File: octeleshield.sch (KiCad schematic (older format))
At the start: 24 parts, among them P1 POWER_HEADER, P2 ANALOG_HEADER, P3 ICSP_HEADER, P4 DIGITAL_HEADER_2, P5 DIGITAL_HEADER_1, P6 V_PROBE2, P7 V_PROBE1, P8 THERMOCOUPLE1, P9 THERMOCOUPLE2, U1 MAX3378E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

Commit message: more work in progress
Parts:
- added C3, C4, C5, C6: 0.1u, Capacitors_SMD:C_0603_HandSoldering, symbol C
- added P7: V_PROBE2_GND, parts:Test_Probe, symbol CONN_01X02
- added P9: V_PROBE1_GND, parts:Test_Probe, symbol CONN_01X02
- C1, C2: footprint (none) -> Capacitors_SMD:C_0603_HandSoldering
- D1, D2, D3, D4: footprint (none) -> Diodes_SMD:SOD-323
- P1, P4, P5: footprint (none) -> Pin_Headers:Pin_Header_Straight_1x08
- P10: renamed from P8; footprint (none) -> parts:Thermocouple
- P11: renamed from P9; footprint (none) -> parts:Thermocouple
- P2: footprint (none) -> Pin_Headers:Pin_Header_Straight_1x06
- P3: footprint (none) -> Socket_Strips:Socket_Strip_Straight_2x03
- P6: value V_PROBE2 -> V_PROBE2_SIG; footprint (none) -> parts:Test_Probe; MFN (none) -> TE Connectivity; MFPN (none) -> 3-582118-2
- P8: renamed from P7; value V_PROBE1 -> V_PROBE1_SIG; footprint (none) -> parts:Test_Probe; MFN (none) -> TE Connectivity; MFPN (none) -> 3-582118-2
- R1, R2, R3, R4, R5, R6: footprint (none) -> Resistors_SMD:R_0603_HandSoldering
- U1: footprint (none) -> Housings_SSOP:TSSOP-14_4.4x5mm_Pitch0.65mm
- U2, U3: footprint SO-8 -> Power_Integrations:SO-8
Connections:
- net +3V3: now also C4.2, C5.2, C6.2
- net +5V: now also P3.5 (P5), C3.1; no longer P3.1 (P1)
- net GND: now also P3.1 (P1), C3.2, C4.1, C5.1, C6.1, P7.1 (P1), P9.1 (P1); no longer P3.5 (P5), P6.2 (P2), P8.2 (P2)
- net MISO: now also P3.6 (P6); no longer P3.2 (P2)
- no-connect marks 23 -> 27

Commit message: work in progress, first try of pcb layout
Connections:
- net +3V3: now also U1.8 (~THREE-STATE)
- net CS1: now also P5.3 (P3); no longer P5.6 (P6)
- net CS2: now also P5.4 (P4); no longer P5.7 (P7)
- net A4: now reaches P2.5 (P5)
- net A4: now also R2.2
- net A5: now reaches P2.6 (P6)
- net A5: now also R1.2
- net A0: no longer names the net of P2.1 (P1)
- net A0: no longer R2.2
- net A1: no longer names the net of P2.2 (P2)
- net A1: no longer R1.2
- net TC_ENABLE: no longer names the net of P5.5 (P5)
- no-connect marks 27 -> 28
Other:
- note added: "4.32:1 voltage divider"
- note added: "Power lines connected to each other within Arduino\n(so e.g. should not wire the two 5V pins to each other)"
- note added: "VCC is higher voltage side, VL is lower voltage side\nThe ~THREE-STATE~ pin is kept high for\nalways normal operation"
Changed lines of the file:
@@
 Sheet 1 1
 Title "Overclocking telemetry shield for Arduino Yún"
-Date "2016-01-11"
+Date "2016-01-17"
 Rev "v1"
 Comp "Moonpunch.org"
@@
 Text Label 6300 2800 2    60   ~ 0
 CS2
-Text Label 6300 2200 2    60   ~ 0
-TC_ENABLE
 Text Label 3050 3650 1    60   ~ 0
 SCLK
@@
 NoConn ~ 4050 2250
 NoConn ~ 4050 2150
-Text Label 4050 3450 0    60   ~ 0
+Text Label 4050 3750 0    60   ~ 0
 CS1
-Text Label 4050 3350 0    60   ~ 0
+Text Label 4050 3650 0    60   ~ 0
 CS2
-Text Label 4050 3550 0    60   ~ 0
-TC_ENABLE
 NoConn ~ 4050 3250
-NoConn ~ 4050 3650
-NoConn ~ 4050 3750
+NoConn ~ 4050 3450
+NoConn ~ 4050 3350
 NoConn ~ 4050 3850
 NoConn ~ 4050 3950
@@
 GND
 NoConn ~ 2000 2950
-Text Label 2000 3850 2    60   ~ 0
-A0
-Text Label 2000 3750 2    60   ~ 0
-A1
+Text Label 2000 3450 2    60   ~ 0
+A4
+Text Label 2000 3350 2    60   ~ 0
+A5
 NoConn ~ 2000 3650
 NoConn ~ 2000 3550
-NoConn ~ 2000 3450
-NoConn ~ 2000 3350
+NoConn ~ 2000 3850
+NoConn ~ 2000 3750
 Text Notes 6150 950  0    157  ~ 31
 Dual thermocouple measurement
 Text Label 7300 5850 2    60   ~ 0
-A0
+A4
 Text Label 7300 4700 2    60   ~ 0
-A1
+A5
 $Comp
 L +5V #PWR01
@@
 NoConn ~ 10100 5950
 NoConn ~ 9450 5950
-Wire Wire Line
-	7600 2350 7850 2350
-Wire Wire Line
-	7850 2350 7850 1500
-Wire Wire Line
-	7850 1500 8450 1500
-Wire Wire Line
-	7800 2350 7800 2900
-Connection ~ 7800 2350
-Wire Wire Line
-	7600 2500 7950 2500
-Wire Wire Line
-	7950 2500 7950 1600
+NoConn ~ 9450 4800
 Wire Wire Line
 	7950 1600 8450 1600
-Wire Wire Line
-	7900 2500 7900 3000
-Connection ~ 7900 2500
 Wire Wire Line
 	7600 2650 8050 2650
@@
 Wire Wire Line
 	10000 4700 10000 4900
-NoConn ~ 9450 4800
+Wire Wire Line
+	7950 2500 7950 1600
+Connection ~ 7900 2500
+Wire Wire Line
+	7600 2500 7950 2500
+Wire Wire Line
+	7900 2500 7900 3000
+Connection ~ 7800 2350
+Wire Wire Line
+	7800 2350 7800 2900
+Wire Wire Line
+	7600 2350 7850 2350
+Wire Wire Line
+	7850 1500 8450 1500
+Wire Wire Line
+	7850 2350 7850 1500
+Text Label 7600 2200 0    60   ~ 0
+3V3
+NoConn ~ 4050 3550
+Text Notes 1650 4600 0    60   ~ 0
+Power lines connected to each other within Arduino\n(so e.g. should not wire the two 5V pins to each other)
+Text Notes 5800 3750 0    60   ~ 0
+VCC is higher voltage side, VL is lower voltage side\nThe ~THREE-STATE~ pin is kept high for\nalways normal operation
+Text Notes 8400 4450 0    60   ~ 0
+4.32:1 voltage divider
 $EndSCHEMATC

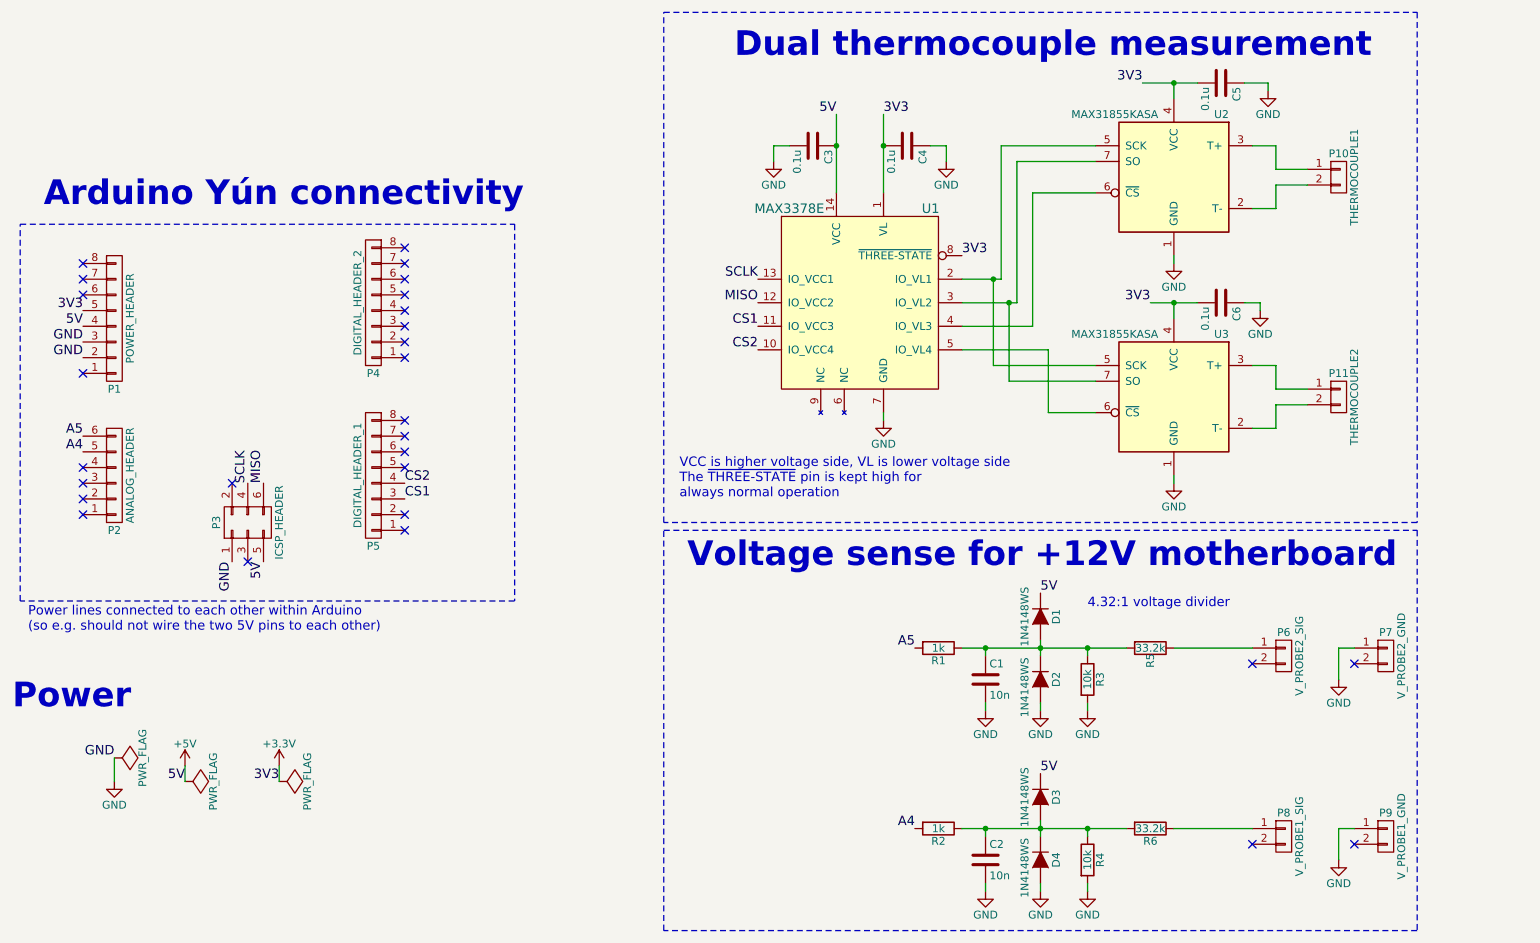
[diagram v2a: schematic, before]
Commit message: some markup and gerber output directory
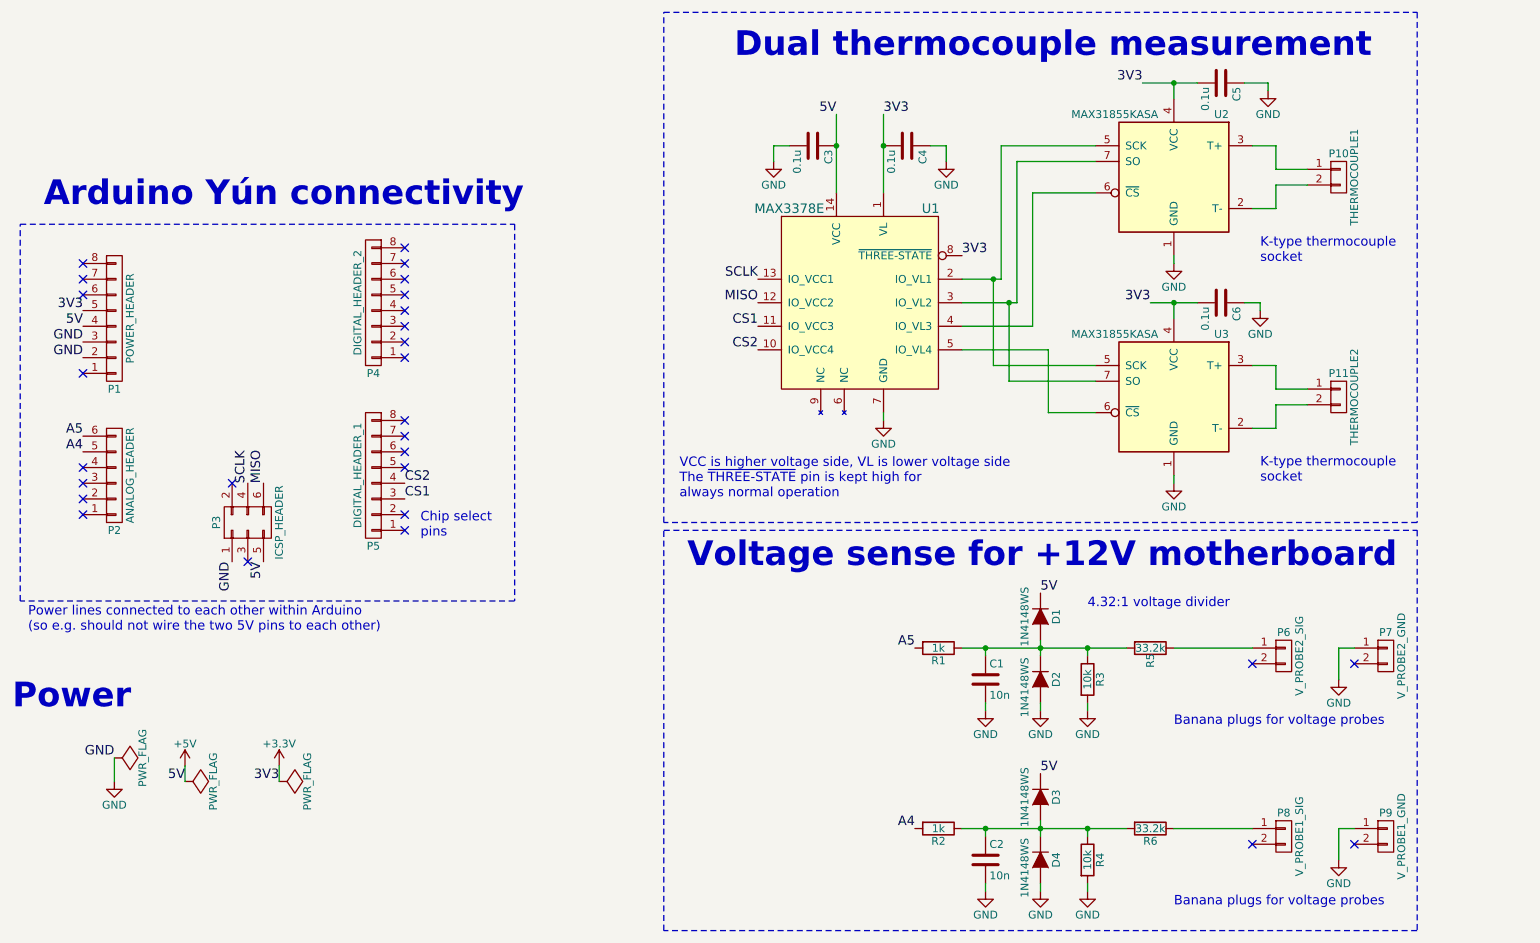
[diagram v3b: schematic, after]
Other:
- note added: "Banana plugs for voltage probes"
- note added: "Banana plugs for voltage probes\n"
- note added: "Chip select\npins"
- note added: "K-type thermocouple\nsocket"
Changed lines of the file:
@@
 Text Notes 8400 4450 0    60   ~ 0
 4.32:1 voltage divider
+Text Notes 8950 5200 0    60   ~ 0
+Banana plugs for voltage probes
+Text Notes 8950 6350 0    60   ~ 0
+Banana plugs for voltage probes\n
+Text Notes 9500 3650 0    60   ~ 0
+K-type thermocouple\nsocket
+Text Notes 9500 2250 0    60   ~ 0
+K-type thermocouple\nsocket
+Text Notes 4150 4000 0    60   ~ 0
+Chip select\npins
 $EndSCHEMATC

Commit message: work in progress, component updates
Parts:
- C1, C2: value 10n -> 100n; MFN (none) -> AVX; MFPN (none) -> 06035C104KAT2A
- C3: value 0.1u -> 100n; MFN (none) -> 06035C104KAT2A; MFPN (none) -> 06035C104KAT2A
- C4: value 0.1u -> 100n; MFN (none) -> AVX; MFPN (none) -> 06035C104KAT2A
- C5, C6: value 0.1u -> 100n
- P10, P11: MFN (none) -> RS Pro; MFPN (none) -> 381-7564; S1L (none) -> http://twen.rs-online.com/web/p/products/3817564/; S1N (none) -> RS Electronics; S1PN (none) -> 381-7564
- R5, R6: value 33.2k -> 33k
- U1: MFN (none) -> Maxim Integrated; MFPN (none) -> MAX3378EEUD+
- U2, U3: value MAX31855KASA -> MAX31855KASA+; MFN (none) -> Maxim Integrated; MFPN (none) -> MAX31855KASA+
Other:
- note added: "4.3:1 voltage divider"
- note removed: "4.32:1 voltage divider"
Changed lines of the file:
@@
 Sheet 1 1
 Title "Overclocking telemetry shield for Arduino Yún"
-Date "2016-01-17"
+Date "2016-02-22"
 Rev "v1"
 Comp "Moonpunch.org"
@@
 P 8950 1700
 F 0 "U2" H 8600 2100 50  0000 L CNN
-F 1 "MAX31855KASA" H 9050 2100 50  0000 L CNN
+F 1 "MAX31855KASA+" H 9050 2100 50  0000 L CNN
 F 2 "Power_Integrations:SO-8" H 8950 1700 50  0001 C CIN
-F 3 "" H 8950 1700 50  0000 C CNN
+F 3 "https://datasheets.maximintegrated.com/en/ds/MAX31855.pdf" H 8950 1700 50  0001 C CNN
+F 4 "Maxim Integrated" H 8950 1700 60  0001 C CNN "MFN"
+F 5 "MAX31855KASA+" H 8950 1700 60  0001 C CNN "MFPN"
 	1    8950 1700
 	-1   0    0    -1
@@
 P 8950 3100
 F 0 "U3" H 8600 3500 50  0000 L CNN
-F 1 "MAX31855KASA" H 9050 3500 50  0000 L CNN
+F 1 "MAX31855KASA+" H 9050 3500 50  0000 L CNN
 F 2 "Power_Integrations:SO-8" H 8950 3100 50  0001 C CIN
-F 3 "" H 8950 3100 50  0000 C CNN
+F 3 "https://datasheets.maximintegrated.com/en/ds/MAX31855.pdf" H 8950 3100 50  0001 C CNN
+F 4 "Maxim Integrated" H 8950 3100 60  0001 C CNN "MFN"
+F 5 "MAX31855KASA+" H 8950 3100 60  0001 C CNN "MFPN"
 	1    8950 3100
 	-1   0    0    -1
@@
 F 2 "parts:Thermocouple" H 10000 1700 50  0001 C CNN
 F 3 "" H 10000 1700 50  0000 C CNN
+F 4 "RS Pro" H 10000 1700 60  0001 C CNN "MFN"
+F 5 "381-7564" H 10000 1700 60  0001 C CNN "MFPN"
+F 6 "RS Electronics" H 10000 1700 60  0001 C CNN "S1N"
+F 7 "381-7564" H 10000 1700 60  0001 C CNN "S1PN"
+F 8 "http://twen.rs-online.com/web/p/products/3817564/" H 10000 1700 60  0001 C CNN "S1L"
 	1    10000 1700
 	1    0    0    -1
@@
 F 2 "parts:Thermocouple" H 10000 3100 50  0001 C CNN
 F 3 "" H 10000 3100 50  0000 C CNN
+F 4 "RS Pro" H 10000 3100 60  0001 C CNN "MFN"
+F 5 "381-7564" H 10000 3100 60  0001 C CNN "MFPN"
+F 6 "RS Electronics" H 10000 3100 60  0001 C CNN "S1N"
+F 7 "381-7564" H 10000 3100 60  0001 C CNN "S1PN"
+F 8 "http://twen.rs-online.com/web/p/products/3817564/" H 10000 3100 60  0001 C CNN "S1L"
 	1    10000 3100
 	1    0    0    -1
@@
 U 1 1 569229CC
 P 8800 4700
-F 0 "R5" H 8880 4700 50  0000 C CNN
-F 1 "33.2k" V 8800 4700 50  0000 C CNN
+F 0 "R5" V 8880 4700 50  0000 C CNN
+F 1 "33k" V 8800 4700 50  0000 C CNN
 F 2 "Resistors_SMD:R_0603_HandSoldering" V 8730 4700 50  0001 C CNN
-F 3 "" H 8800 4700 50  0000 C CNN
+F 3 "http://www.yageo.com/NewPortal/yageodocoutput?fileName=/pdf/R-Chip/PYu-RT_1-to-0.05_RoHS_L_6.pdf" H 8800 4700 50  0001 C CNN
 	1    8800 4700
 	0    1    1    0
@@
 F 1 "10k" V 8400 4900 50  0000 C CNN
 F 2 "Resistors_SMD:R_0603_HandSoldering" V 8330 4900 50  0001 C CNN
-F 3 "" H 8400 4900 50  0000 C CNN
+F 3 "http://www.yageo.com/NewPortal/yageodocoutput?fileName=/pdf/R-Chip/PYu-RT_1-to-0.05_RoHS_L_6.pdf" H 8400 4900 50  0001 C CNN
 	1    8400 4900
 	1    0    0    -1
@@
 F 1 "1k" V 7450 4700 50  0000 C CNN
 F 2 "Resistors_SMD:R_0603_HandSoldering" V 7380 4700 50  0001 C CNN
-F 3 "" H 7450 4700 50  0000 C CNN
+F 3 "http://www.yageo.com/NewPortal/yageodocoutput?fileName=/pdf/R-Chip/PYu-RT_1-to-0.05_RoHS_L_6.pdf" H 7450 4700 50  0001 C CNN
 	1    7450 4700
 	0    1    1    0
@@
 P 8800 5850
 F 0 "R6" V 8880 5850 50  0000 C CNN
-F 1 "33.2k" V 8800 5850 50  0000 C CNN
+F 1 "33k" V 8800 5850 50  0000 C CNN
 F 2 "Resistors_SMD:R_0603_HandSoldering" V 8730 5850 50  0001 C CNN
-F 3 "" H 8800 5850 50  0000 C CNN
+F 3 "http://www.yageo.com/NewPortal/yageodocoutput?fileName=/pdf/R-Chip/PYu-RT_1-to-0.05_RoHS_L_6.pdf" H 8800 5850 50  0001 C CNN
 	1    8800 5850
 	0    1    1    0
@@
 F 1 "10k" V 8400 6050 50  0000 C CNN
 F 2 "Resistors_SMD:R_0603_HandSoldering" V 8330 6050 50  0001 C CNN
-F 3 "" H 8400 6050 50  0000 C CNN
+F 3 "http://www.yageo.com/NewPortal/yageodocoutput?fileName=/pdf/R-Chip/PYu-RT_1-to-0.05_RoHS_L_6.pdf" H 8400 6050 50  0001 C CNN
 	1    8400 6050
 	1    0    0    -1
@@
 F 1 "1k" V 7450 5850 50  0000 C CNN
 F 2 "Resistors_SMD:R_0603_HandSoldering" V 7380 5850 50  0001 C CNN
-F 3 "" H 7450 5850 50  0000 C CNN
+F 3 "http://www.yageo.com/NewPortal/yageodocoutput?fileName=/pdf/R-Chip/PYu-RT_1-to-0.05_RoHS_L_6.pdf" H 7450 5850 50  0001 C CNN
 	1    7450 5850
 	0    1    1    0
@@
 P 7750 4900
 F 0 "C1" H 7775 5000 50  0000 L CNN
-F 1 "10n" H 7775 4800 50  0000 L CNN
+F 1 "100n" H 7775 4800 50  0000 L CNN
 F 2 "Capacitors_SMD:C_0603_HandSoldering" H 7788 4750 50  0001 C CNN
-F 3 "" H 7750 4900 50  0000 C CNN
+F 3 "http://www.mouser.com/ds/2/40/X7RDielectric-777024.pdf" H 7750 4900 50  0001 C CNN
+F 4 "AVX" H 7750 4900 60  0001 C CNN "MFN"
+F 5 "06035C104KAT2A" H 7750 4900 60  0001 C CNN "MFPN"
 	1    7750 4900
 	1    0    0    -1
@@
 P 7750 6050
 F 0 "C2" H 7775 6150 50  0000 L CNN
-F 1 "10n" H 7775 5950 50  0000 L CNN
+F 1 "100n" H 7775 5950 50  0000 L CNN
 F 2 "Capacitors_SMD:C_0603_HandSoldering" H 7788 5900 50  0001 C CNN
-F 3 "" H 7750 6050 50  0000 C CNN
+F 3 "http://www.mouser.com/ds/2/40/X7RDielectric-777024.pdf" H 7750 6050 50  0001 C CNN
+F 4 "AVX" H 7750 6050 60  0001 C CNN "MFN"
+F 5 "06035C104KAT2A" H 7750 6050 60  0001 C CNN "MFPN"
 	1    7750 6050
 	1    0    0    -1
@@
 F 1 "MAX3378E" H 7400 2900 60  0000 C CNN
 F 2 "Housings_SSOP:TSSOP-14_4.4x5mm_Pitch0.65mm" H 6950 2400 60  0001 C CNN
-F 3 "" H 6950 2400 60  0000 C CNN
+F 3 "https://datasheets.maximintegrated.com/en/ds/MAX3372E-MAX3393E.pdf" H 6950 2400 60  0001 C CNN
+F 4 "Maxim Integrated" H 6950 2400 60  0001 C CNN "MFN"
+F 5 "MAX3378EEUD+" H 6950 2400 60  0001 C CNN "MFPN"
 	1    6950 2400
 	-1   0    0    -1
@@
 P 6650 1500
 F 0 "C3" H 6675 1600 50  0000 L CNN
-F 1 "0.1u" H 6675 1400 50  0000 L CNN
+F 1 "100n" H 6675 1400 50  0000 L CNN
 F 2 "Capacitors_SMD:C_0603_HandSoldering" H 6688 1350 50  0001 C CNN
-F 3 "" H 6650 1500 50  0000 C CNN
+F 3 "http://www.mouser.com/ds/2/40/X7RDielectric-777024.pdf" H 6650 1500 50  0001 C CNN
+F 4 "06035C104KAT2A" H 6650 1500 60  0001 C CNN "MFN"
+F 5 "06035C104KAT2A" H 6650 1500 60  0001 C CNN "MFPN"
 	1    6650 1500
 	0    1    1    0
@@
 P 7250 1500
 F 0 "C4" H 7275 1600 50  0000 L CNN
-F 1 "0.1u" H 7275 1400 50  0000 L CNN
+F 1 "100n" H 7275 1400 50  0000 L CNN
 F 2 "Capacitors_SMD:C_0603_HandSoldering" H 7288 1350 50  0001 C CNN
-F 3 "" H 7250 1500 50  0000 C CNN
+F 3 "http://www.mouser.com/ds/2/40/X7RDielectric-777024.pdf" H 7250 1500 50  0001 C CNN
+F 4 "AVX" H 7250 1500 60  0001 C CNN "MFN"
+F 5 "06035C104KAT2A" H 7250 1500 60  0001 C CNN "MFPN"
 	1    7250 1500
 	0    1    1    0
@@
 P 9250 1100
 F 0 "C5" H 9275 1200 50  0000 L CNN
-F 1 "0.1u" H 9275 1000 50  0000 L CNN
+F 1 "100n" H 9275 1000 50  0000 L CNN
 F 2 "Capacitors_SMD:C_0603_HandSoldering" H 9288 950 50  0001 C CNN
 F 3 "" H 9250 1100 50  0000 C CNN
@@
 P 9250 2500
 F 0 "C6" H 9275 2600 50  0000 L CNN
-F 1 "0.1u" H 9275 2400 50  0000 L CNN
+F 1 "100n" H 9275 2400 50  0000 L CNN
 F 2 "Capacitors_SMD:C_0603_HandSoldering" H 9288 2350 50  0001 C CNN
 F 3 "" H 9250 2500 50  0000 C CNN
@@
 VCC is higher voltage side, VL is lower voltage side\nThe ~THREE-STATE~ pin is kept high for\nalways normal operation
 Text Notes 8400 4450 0    60   ~ 0
-4.32:1 voltage divider
+4.3:1 voltage divider
 Text Notes 8950 5200 0    60   ~ 0
 Banana plugs for voltage probes

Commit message: more work in progress, getting there
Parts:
- P6: value V_PROBE2_SIG -> V_PROBE1_SIG
- P7: value V_PROBE2_GND -> V_PROBE1_GND
- P8: value V_PROBE1_SIG -> V_PROBE2_SIG
- P9: value V_PROBE1_GND -> V_PROBE2_GND
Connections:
- net A4 renamed A1
- net A5 renamed A0
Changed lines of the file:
@@
 P 9650 4750
 F 0 "P6" H 9650 4900 50  0000 C CNN
-F 1 "V_PROBE2_SIG" V 9750 4750 50  0000 C CNN
+F 1 "V_PROBE1_SIG" V 9750 4750 50  0000 C CNN
 F 2 "parts:Test_Probe" H 9650 4750 50  0001 C CNN
 F 3 "" H 9650 4750 50  0000 C CNN
@@
 P 9650 5900
 F 0 "P8" H 9650 6050 50  0000 C CNN
-F 1 "V_PROBE1_SIG" V 9750 5900 50  0000 C CNN
+F 1 "V_PROBE2_SIG" V 9750 5900 50  0000 C CNN
 F 2 "parts:Test_Probe" H 9650 5900 50  0001 C CNN
 F 3 "" H 9650 5900 50  0000 C CNN
@@
 NoConn ~ 2000 2950
 Text Label 2000 3450 2    60   ~ 0
-A4
+A1
 Text Label 2000 3350 2    60   ~ 0
-A5
+A0
 NoConn ~ 2000 3650
 NoConn ~ 2000 3550
@@
 Dual thermocouple measurement
 Text Label 7300 5850 2    60   ~ 0
-A4
+A1
 Text Label 7300 4700 2    60   ~ 0
-A5
+A0
 $Comp
 L +5V #PWR01
@@
 P 10300 4750
 F 0 "P7" H 10300 4900 50  0000 C CNN
-F 1 "V_PROBE2_GND" V 10400 4750 50  0000 C CNN
+F 1 "V_PROBE1_GND" V 10400 4750 50  0000 C CNN
 F 2 "parts:Test_Probe" H 10300 4750 50  0001 C CNN
 F 3 "" H 10300 4750 50  0000 C CNN
@@
 P 10300 5900
 F 0 "P9" H 10300 6050 50  0000 C CNN
-F 1 "V_PROBE1_GND" V 10400 5900 50  0000 C CNN
+F 1 "V_PROBE2_GND" V 10400 5900 50  0000 C CNN
 F 2 "parts:Test_Probe" H 10300 5900 50  0001 C CNN
 F 3 "" H 10300 5900 50  0000 C CNN
